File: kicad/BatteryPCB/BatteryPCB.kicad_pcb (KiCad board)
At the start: 2 copper layers, 91 x 63 mm, 29 parts, among them J1 USB4105-GF-A, J2 Conn_01x02_Pin, J3 Conn_01x02_Pin, J4 Conn_01x02_Pin, SW7 SS-12D00-G 4 E, U5 TPS7A4901DGNT, U7 MT3608, U8 TP4056

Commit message: Battery PCB "DRC Clean"
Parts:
- added J5: 5V, Connector_PinSocket_2.54mm:PinSocket_1x02_P2.54mm_Vertical, F.Cu at (70.5, 107.8)
- J2: value Conn_01x02_Pin -> BoostV
- J3: value Conn_01x02_Pin -> BatteryV
- J4: value Conn_01x02_Pin -> 24V
- moved J4 51.6 mm to (143.3, 116.0), turned to -90 degrees
- moved J1 48.3 mm to (59.0, 111.2), turned to -90 degrees
- moved R14 43.6 mm to (71.9, 116.4)
- moved R12 42.6 mm to (135.5, 117.5), turned to 180 degrees
- moved D3 41.1 mm to (77.0, 110.0), turned to 0 degrees
- moved R21 40.4 mm to (66.5, 111.8), turned to -90 degrees
- moved U8 40.2 mm to (77.4, 114.9)
- moved D4 39.5 mm to (77.0, 108.0), turned to 0 degrees
- moved R13 39.0 mm to (135.5, 114.5), turned to 0 degrees
- moved C9 38.1 mm to (83.5, 114.5), turned to 0 degrees
- moved C8 37.6 mm to (83.4, 116.9)
- moved C4 37.5 mm to (96.5, 114.5), turned to -90 degrees
- moved R22 36.8 mm to (66.5, 116.2), turned to -90 degrees
- moved SW7 35.6 mm to (90.5, 108.5)
- moved L1 35.0 mm to (101.0, 116.5), turned to 180 degrees
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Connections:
- net 24V renamed +24V
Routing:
- net Net-(BT1-Pad1): track 0.00 -> 50.5 mm, vias 0 -> 1
- net Battery_Voltage: track 18.1 -> 59.1 mm
- net /Battery&Charging/VBUS_USB: track 27.4 -> 43.2 mm
- net GND: track 0.00 -> 13.6 mm, vias 0 -> 2
- net +24V: track 6.01 -> 18.0 mm
- net Net-(U8-BAT): track 6.63 -> 18.4 mm
- net /Battery&Charging/Boost_LDO_Point: track 23.7 -> 32.8 mm
- net Net-(U8-PROG): track 2.13 -> 7.75 mm
- net Net-(D3-PadA): track 2.19 -> 7.02 mm, vias 0 -> 2
- net Net-(D4-PadA): track 2.40 -> 6.81 mm, vias 0 -> 2
- net Net-(U8-~{CHRG}): track 2.26 -> 6.27 mm
- net Net-(D9-A): track 3.48 -> 6.91 mm
- net Net-(J1-CC1): track 2.62 -> 4.96 mm
- net Net-(J1-CC2): track 3.03 -> 4.95 mm
- net Net-(U5-NR/SS): track 2.44 -> 3.75 mm
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- added copper zone on F.Cu, net GND
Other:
- board size 91 x 63 mm -> 91 x 41.5 mm
- board text added: "24V"
- board text added: "5V"
- board text added: "Batt"
- board text added: "Boost"
- board text added: "Charge <-> Power"
- board text added: "GND"

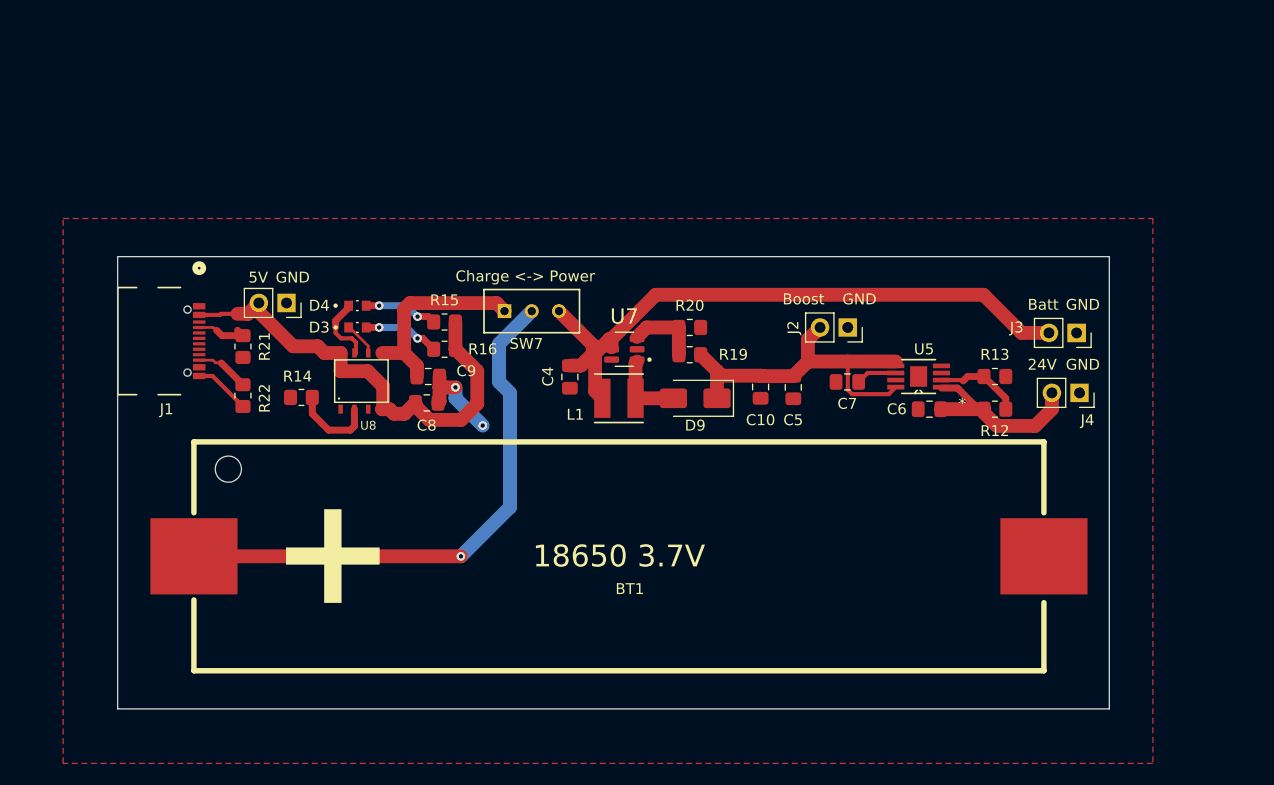
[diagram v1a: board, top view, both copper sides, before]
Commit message: Add mounting holes and 3 pin JST header for interPCB connection
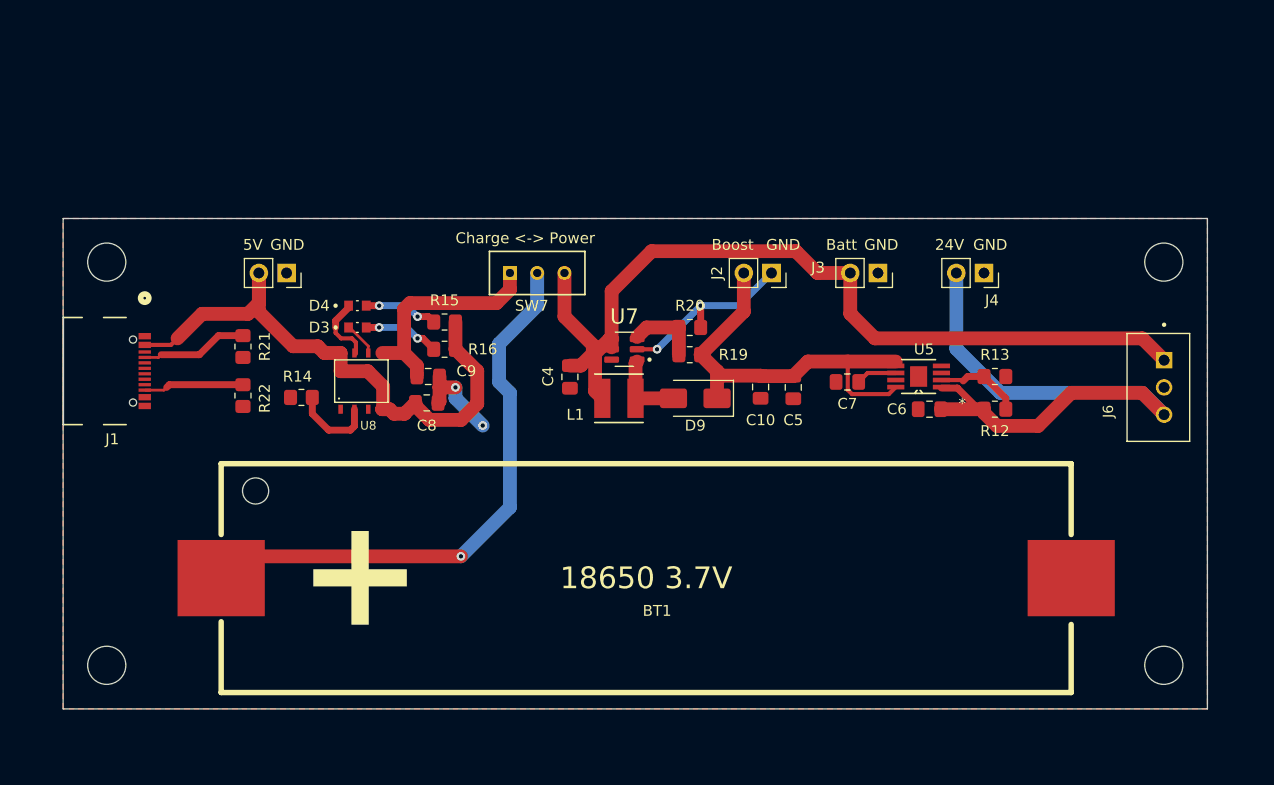
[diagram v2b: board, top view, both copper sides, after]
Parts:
- added H1: MountingHole, MountingHole:MountingHole_3.5mm, F.Cu at (151.0, 104.0)
- added H2: MountingHole, MountingHole:MountingHole_3.5mm, F.Cu at (54.0, 104.0)
- added H3: MountingHole, MountingHole:MountingHole_3.5mm, F.Cu at (54.0, 141.0)
- added H4: MountingHole, MountingHole:MountingHole_3.5mm, F.Cu at (151.0, 141.0)
- added J6: B3B-XH-A, B3B_XH_A:JST_B3B-XH-A, F.Cu at (150.5, 115.5)
- moved J3 19.0 mm to (124.8, 105.0)
- moved J4 14.1 mm to (134.5, 105.0)
- moved J2 8.60 mm to (115.0, 105.0)
- moved J1 5.71 mm to (54.0, 114.0)
- moved SW7 3.54 mm to (91.0, 105.0)
- moved BT1 3.20 mm to (103.5, 133.0)
- moved J5 2.75 mm to (70.5, 105.0)
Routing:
- net +24V: track 18.0 -> 56.7 mm
- net Battery_Voltage: track 59.1 -> 82.1 mm
- net GND: track 13.6 -> 25.7 mm, vias 2 -> 4
- net /Battery&Charging/VBUS_USB: track 43.2 -> 54.8 mm
- net /Battery&Charging/Boost_LDO_Point: track 32.8 -> 38.3 mm
- net Net-(J1-CC1): track 4.96 -> 9.84 mm
- net Net-(J1-CC2): track 4.95 -> 9.22 mm
- net Net-(U8-BAT): track 18.4 -> 20.7 mm
- net Net-(BT1-Pad1): track 50.5 -> 52.6 mm
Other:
- board size 91 x 41.5 mm -> 105 x 45 mm

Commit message: Changed switch and modified passive component values
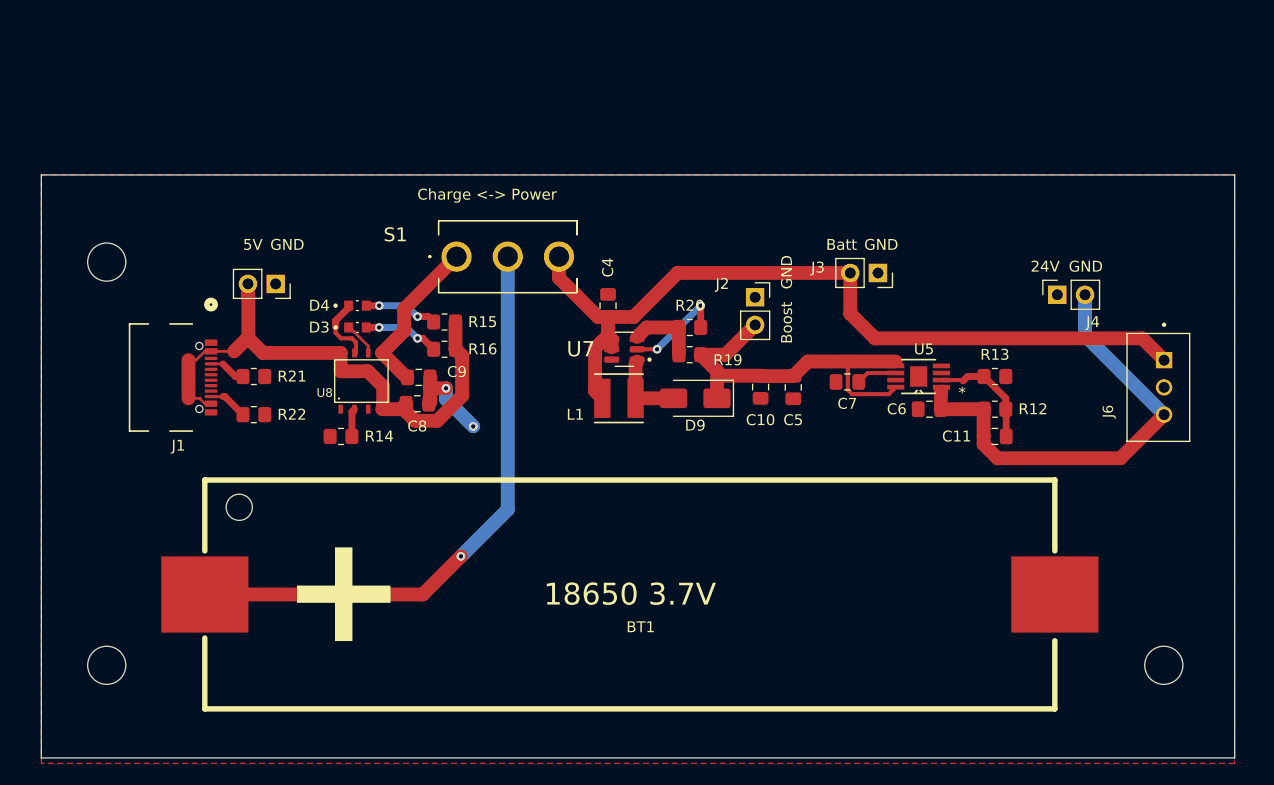
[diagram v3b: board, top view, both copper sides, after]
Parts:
- removed H1: MountingHole, MountingHole:MountingHole_3.5mm
- removed SW7: SS-12D00-G 4 E, ul_SS-12D00-G-4-E:1P2T_SS-12D00_CNK
- added C11: 10nF, Capacitor_SMD:C_0805_2012Metric_Pad1.18x1.45mm_HandSolder, F.Cu at (135.5, 120.0)
- added S1: 500SSP1S1M2QEA, 500SSP1S1M2QEA:500SSP1S1M2QEA, F.Cu at (86.1, 103.5)
- C4, C5: value 10µF -> 22µF
- L1: value 4.7µH -> 10µH
- R19: value 412k -> 422k
- moved C4 7.42 mm to (100.0, 108.0), turned to 90 degrees
- moved J4 7.02 mm to (141.2, 107.0), turned to 90 degrees
- moved J1 6.11 mm to (60.1, 114.6)
- moved R14 5.10 mm to (75.5, 120.0)
- moved R21 2.93 mm to (67.5, 114.5), turned to 0 degrees
- moved J2 2.69 mm to (113.5, 107.2), turned to 0 degrees
- moved BT1 2.12 mm to (102.0, 134.5)
- moved R22 2.02 mm to (67.5, 118.0), turned to 0 degrees
- moved J5 1.41 mm to (69.5, 106.0)
- moved C8 0.87 mm to (82.5, 117.0)
- moved C9 0.87 mm to (82.6, 114.6)
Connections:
- J1 pad B4-A9: unconnected-(J1-VBUS-PadB4-A9) -> /Battery&Charging/VBUS_USB
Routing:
- net +24V: track 56.7 -> 41.6 mm
- net GND: track 25.7 -> 18.0 mm
- net Net-(J1-CC1): track 9.84 -> 3.41 mm
- net Battery_Voltage: track 82.1 -> 75.8 mm
- net Net-(S1-NC): track 20.7 -> 14.9 mm
- net Net-(J1-CC2): track 9.22 -> 3.62 mm
- net Net-(U8-PROG): track 7.75 -> 2.65 mm
- net /Battery&Charging/VBUS_USB: track 54.8 -> 50.9 mm
- net /Battery&Charging/Boost_LDO_Point: track 38.3 -> 35.3 mm
- net Net-(U5-FB): track 8.40 -> 10.9 mm
- net Net-(S1-COM): track 52.6 -> 54.2 mm
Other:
- board size 105 x 45 mm -> 109.5 x 53.5 mm

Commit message: Modified boost converter traces
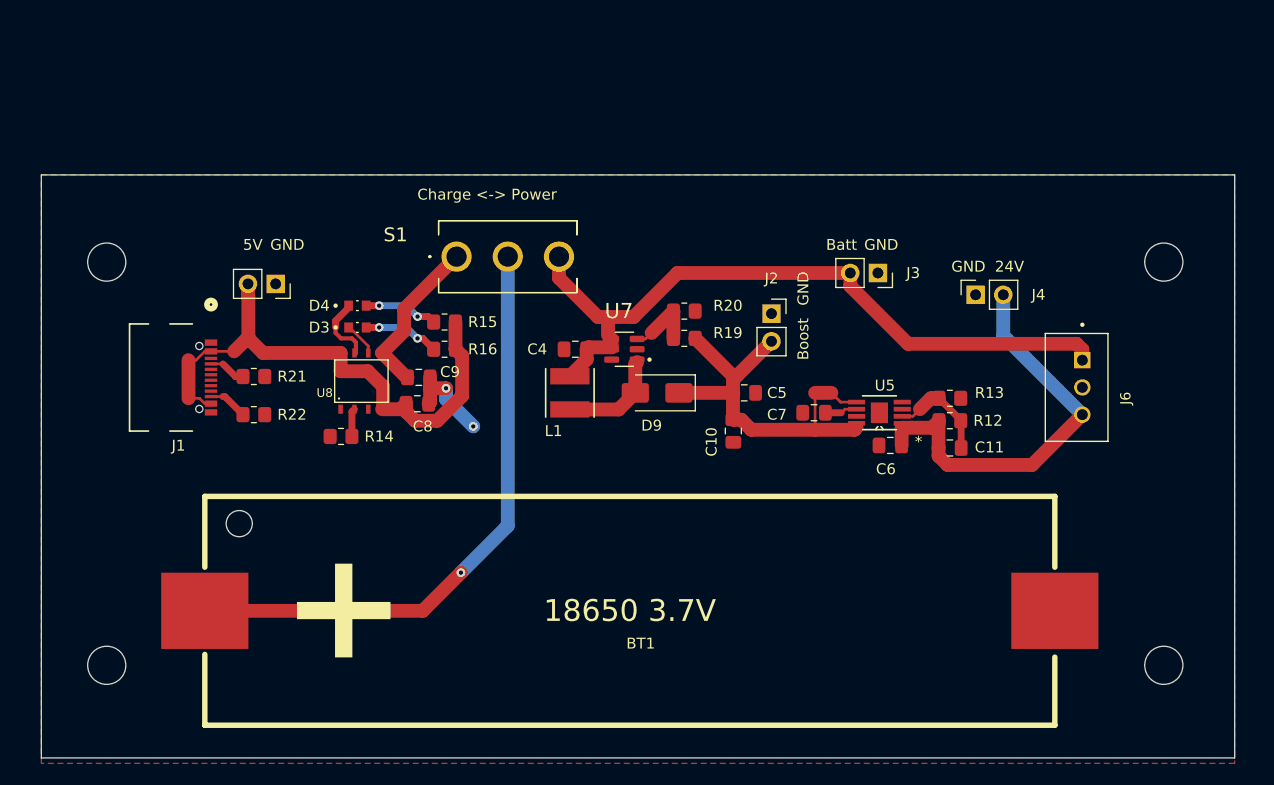
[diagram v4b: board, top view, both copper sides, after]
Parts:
- added H1: MountingHole, MountingHole:MountingHole_3.5mm, F.Cu at (151.0, 104.0)
- moved J4 7.50 mm to (133.7, 107.0)
- moved J6 7.50 mm to (143.0, 115.5)
- moved C4 5.00 mm to (97.0, 112.0), turned to 180 degrees
- moved C6 4.90 mm to (125.9, 120.8)
- moved U5 4.90 mm to (124.9, 117.8)
- moved C10 4.75 mm to (111.5, 119.5)
- moved R13 4.59 mm to (131.4, 116.5)
- moved C5 4.53 mm to (112.5, 116.0), turned to 0 degrees
- moved L1 4.53 mm to (96.5, 116.0), turned to 90 degrees
- moved C11 4.27 mm to (131.4, 121.1)
- moved R12 4.27 mm to (131.4, 118.6)
- moved C7 4.16 mm to (118.9, 117.8)
- moved D9 3.54 mm to (104.5, 116.0)
- moved J2 2.12 mm to (115.0, 108.7)
- moved R19 1.58 mm to (107.0, 111.0)
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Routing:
- net Battery_Voltage: track 75.8 -> 65.7 mm
- net GND: track 18.0 -> 8.47 mm, vias 4 -> 2
- net +24V: track 41.6 -> 37.9 mm
- net /Battery&Charging/Boost_LDO_Point: track 35.3 -> 38.2 mm
- net Net-(D9-A): track 6.91 -> 9.53 mm
- net Net-(S1-COM): track 54.2 -> 55.7 mm
- net Net-(U5-FB): track 10.9 -> 9.45 mm
- net Net-(U5-NR/SS): track 3.75 -> 3.00 mm

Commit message: Final PCB
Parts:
- removed BT1: BK-18650-PC2, FreddyBattery:BH-18650-B1BA002
- removed H3, H4: MountingHole, MountingHole:MountingHole_3.5mm
- removed U8: TP4056, TP4056:SOT23-8
- added U1: TP4056, TP4056:SOP127P600X175-9N, F.Cu at (68.5, 115.5)
- L1: value 10µH -> VLS6045EX-100M; footprint SRN4018_4R7M:IND_BOURNS_SRN4018 -> VLS6045EX_100M:IND_VLS6045EX-100M
- R16: value 1k -> 470
- moved H1 17.0 mm to (134.5, 100.0)
- moved J4 11.4 mm to (122.5, 105.5)
- moved J6 10.8 mm to (133.0, 111.5)
- moved R21 10.1 mm to (57.5, 116.0)
- moved R22 10.0 mm to (57.5, 118.5)
- moved J1 9.82 mm to (50.3, 115.0)
- moved L1 9.62 mm to (87.0, 117.5), turned to -90 degrees
- moved C9 8.98 mm to (73.7, 115.1)
- moved C10 8.98 mm to (102.5, 120.0)
- moved C4 8.98 mm to (88.0, 112.5)
- moved C5 8.98 mm to (103.5, 116.5)
- moved C6 8.98 mm to (116.9, 121.4)
- moved C7 8.98 mm to (109.9, 118.4)
- moved C8 8.98 mm to (73.5, 117.5)
- moved D3 8.98 mm to (68.0, 110.5)
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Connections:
- D3 pad C: Net-(U8-~{STDBY}) -> /Battery&Charging/STDBY
- D4 pad C: Net-(U8-~{CHRG}) -> /Battery&Charging/CHRG
- L1 pad 1: Net-(D9-A) -> Battery_Voltage
- L1 pad 2: Battery_Voltage -> Net-(D9-A)
- U7 pad 6: (no net) -> unconnected-(U7-NC-Pad6)
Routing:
- net Net-(S1-COM): track 55.7 -> 44.2 mm, vias 1 -> 0
- net /Battery&Charging/VBUS_USB: track 50.9 -> 57.6 mm, vias 0 -> 2
- net /Battery&Charging/CHRG: track 0.00 -> 6.27 mm
- net Net-(U8-~{CHRG}): track 6.27 -> 0.00 mm
- net Net-(U8-~{STDBY}): track 3.15 -> 0.00 mm
- net /Battery&Charging/STDBY: track 0.00 -> 3.15 mm
- net Battery_Voltage: track 65.7 -> 63.9 mm
- net Net-(D4-PadA): track 6.81 -> 8.32 mm
- net /Battery&Charging/Boost_LDO_Point: track 38.2 -> 36.9 mm
- net Net-(D9-A): track 9.53 -> 10.7 mm
- net +24V: track 37.9 -> 37.1 mm
- net GND: vias 2 -> 3
- added copper zone on B.Cu, net GND
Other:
- board size 109.5 x 53.5 mm -> 95.8 x 49.5 mm

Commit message: Added skull
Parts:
- added BT1: BK-18650-PC2, FreddyBattery:BH-18650-B1BA002, B.Cu at (96.0, 131.0)
